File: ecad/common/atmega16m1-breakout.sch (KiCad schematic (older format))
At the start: 17 parts, among them J1 Conn_01x15, J2 Conn_01x15, J3 Conn_02x03_Odd_Even, SW1 SW_Push, U1 ATMEGA16M1-AU, U2 NCP1117-5.0_SOT223, Y1 16MHz

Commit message: wip
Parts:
- removed J1, J2: Conn_01x15, Pin_Headers:Pin_Header_Straight_1x15_Pitch2.54mm, symbol Conn_01x15
- added C9: 100nF, Capacitors_SMD:C_0603, symbol C
- added J?: Conn_01x08, symbol Conn_01x08
- added J?: Conn_01x03, symbol Conn_01x03
- added J? (x2): Conn_01x06, symbol Conn_01x06
- added J?: Conn_01x05, symbol Conn_01x05
- added U3: MCP2561-E/SN, Housings_SOIC:SOIC-8_3.9x4.9mm_Pitch1.27mm, symbol MCP2561-E/SN
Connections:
- net labels added: CAN+, CAN-, RXCAN, TXCAN
- net labels removed: 6, 7
- wire segments 123 -> 135
- no-connect marks 1 -> 2

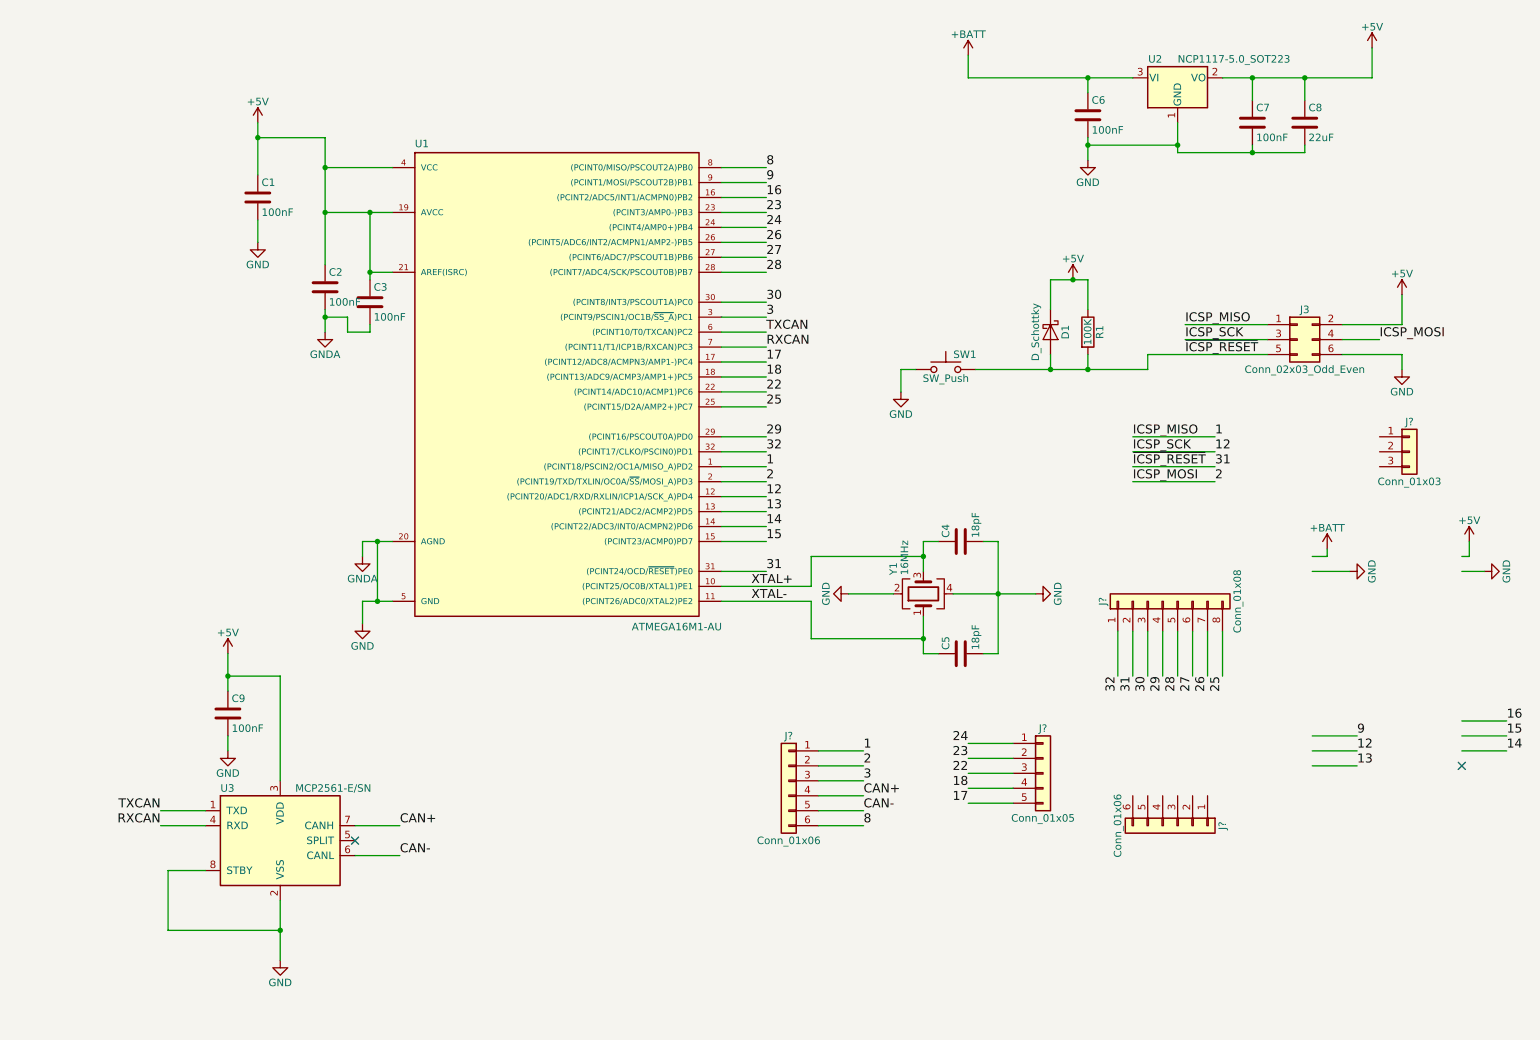
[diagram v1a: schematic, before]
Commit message: Adds CAN Transceiver on atmega16m1 breakout
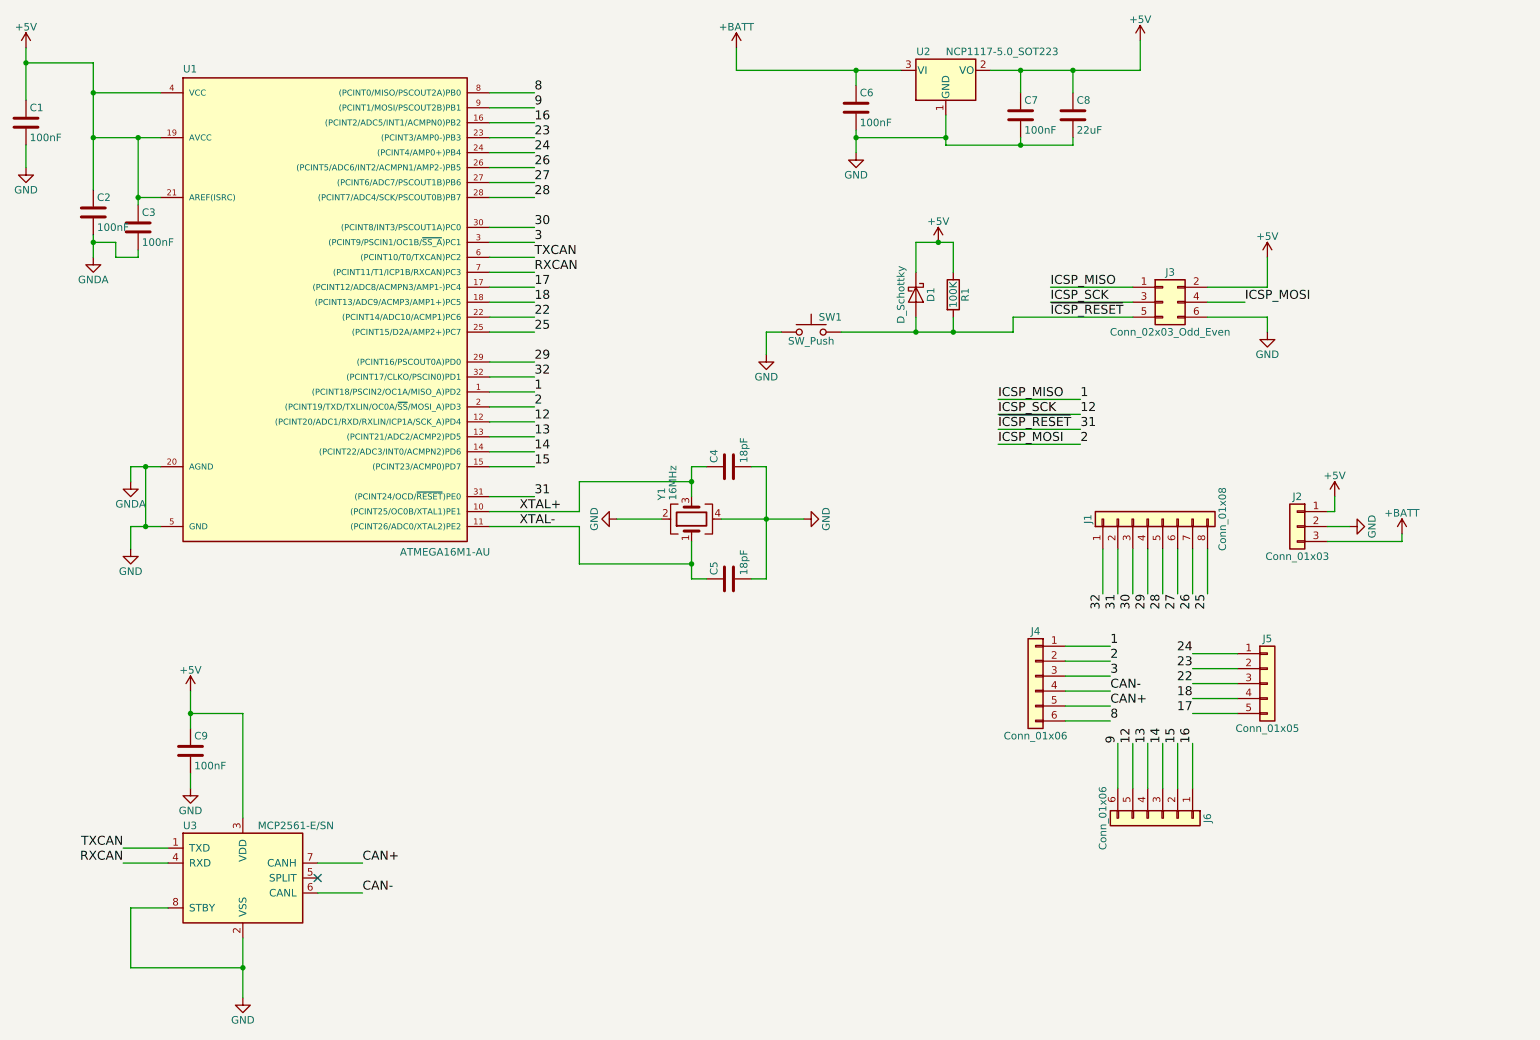
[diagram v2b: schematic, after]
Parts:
- J1: renamed from J?; footprint (none) -> Pin_Headers:Pin_Header_Straight_1x08_Pitch2.54mm
- J2: renamed from J?; footprint (none) -> Pin_Headers:Pin_Header_Straight_1x03_Pitch2.54mm
- J4, J6: renamed from J?; footprint (none) -> Pin_Headers:Pin_Header_Straight_1x06_Pitch2.54mm
- J5: renamed from J?; footprint (none) -> Pin_Headers:Pin_Header_Straight_1x05_Pitch2.54mm
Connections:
- wire segments 135 -> 134
- no-connect marks 2 -> 1
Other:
- moved on the sheet: C1, C2, C3, C4, C5, C6, C7, C8, C9, D1, J1, J2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

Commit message: Updates breakout board
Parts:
- C1, C2, C3, C6, C7, C9: Part Number (none) -> 06035C104KAT2A
- C4, C5: Part Number (none) -> 06031A180KAT2A
- D1: Part Number (none) -> BAT54
- R1: Part Number (none) -> RMCF0603FT10K0
- SW1: Part Number (none) -> 1825910-6
- Y1: Part Number (none) -> FA-238 16.0000MB-C3
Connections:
- net GND: now also C4.1; no longer C4.2
- net XTAL+: now also C4.2; no longer C4.1
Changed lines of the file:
@@
 F 2 "Capacitors_SMD:C_0603" H 888 1200 50  0001 C CNN
 F 3 "" H 850 1350 50  0001 C CNN
+F 4 "06035C104KAT2A" H 850 1350 60  0001 C CNN "Part Number"
 	1    850  1350
 	1    0    0    -1
@@
 F 2 "Capacitors_SMD:C_0603" H 1338 1800 50  0001 C CNN
 F 3 "" H 1300 1950 50  0001 C CNN
+F 4 "06035C104KAT2A" H 1300 1950 60  0001 C CNN "Part Number"
 	1    1300 1950
 	1    0    0    -1
@@
 F 2 "Capacitors_SMD:C_0603" H 1638 1900 50  0001 C CNN
 F 3 "" H 1600 2050 50  0001 C CNN
+F 4 "06035C104KAT2A" H 1600 2050 60  0001 C CNN "Part Number"
 	1    1600 2050
 	1    0    0    -1
@@
 	1300 1450 1750 1450
 $Comp
-L +5V #PWR2
+L +5V #PWR01
 U 1 1 5B852E50
 P 850 850
-F 0 "#PWR2" H 850 700 50  0001 C CNN
+F 0 "#PWR01" H 850 700 50  0001 C CNN
 F 1 "+5V" H 850 990 50  0000 C CNN
 F 2 "" H 850 850 50  0001 C CNN
@@
 Connection ~ 850  950
 $Comp
-L GND #PWR5
+L GND #PWR02
 U 1 1 5B852E84
 P 850 1650
-F 0 "#PWR5" H 850 1400 50  0001 C CNN
+F 0 "#PWR02" H 850 1400 50  0001 C CNN
 F 1 "GND" H 850 1500 50  0000 C CNN
 F 2 "" H 850 1650 50  0001 C CNN
@@
 	850  1650 850  1500
 $Comp
-L GNDA #PWR7
+L GNDA #PWR03
 U 1 1 5B852EBB
 P 1300 2250
-F 0 "#PWR7" H 1300 2000 50  0001 C CNN
+F 0 "#PWR03" H 1300 2000 50  0001 C CNN
 F 1 "GNDA" H 1300 2100 50  0000 C CNN
 F 2 "" H 1300 2250 50  0001 C CNN
@@
 Connection ~ 1300 2150
 $Comp
-L GND #PWR17
+L GND #PWR04
 U 1 1 5B852F69
 P 1550 4200
-F 0 "#PWR17" H 1550 3950 50  0001 C CNN
+F 0 "#PWR04" H 1550 3950 50  0001 C CNN
 F 1 "GND" H 1550 4050 50  0000 C CNN
 F 2 "" H 1550 4200 50  0001 C CNN
@@
 $EndComp
 $Comp
-L GNDA #PWR11
+L GNDA #PWR05
 U 1 1 5B852F94
 P 1550 3750
-F 0 "#PWR11" H 1550 3500 50  0001 C CNN
+F 0 "#PWR05" H 1550 3500 50  0001 C CNN
 F 1 "GNDA" H 1550 3600 50  0000 C CNN
 F 2 "" H 1550 3750 50  0001 C CNN
@@
 F 2 "Crystals:Crystal_SMD_SeikoEpson_FA238-4pin_3.2x2.5mm_HandSoldering" H 5300 4000 50  0001 C CNN
 F 3 "" H 5300 4000 50  0001 C CNN
+F 4 "FA-238 16.0000MB-C3" H 5300 4000 60  0001 C CNN "Part Number"
 	1    5300 4000
 	0    -1   -1   0
@@
 F 2 "Capacitors_SMD:C_0603" H 5588 3500 50  0001 C CNN
 F 3 "" H 5550 3650 50  0001 C CNN
+F 4 "06031A180KAT2A" H 5550 3650 60  0001 C CNN "Part Number"
 	1    5550 3650
-	0    -1   -1   0
+	0    1    1    0
 $EndComp
 $Comp
@@
 F 2 "Capacitors_SMD:C_0603" H 5588 4250 50  0001 C CNN
 F 3 "" H 5550 4400 50  0001 C CNN
+F 4 "06031A180KAT2A" H 5550 4400 60  0001 C CNN "Part Number"
 	1    5550 4400
 	0    -1   -1   0
@@
 Connection ~ 5800 4000
 $Comp
-L GND #PWR14
+L GND #PWR06
 U 1 1 5B853598
 P 6050 4000
-F 0 "#PWR14" H 6050 3750 50  0001 C CNN
+F 0 "#PWR06" H 6050 3750 50  0001 C CNN
 F 1 "GND" H 6050 3850 50  0000 C CNN
 F 2 "" H 6050 4000 50  0001 C CNN
@@
 Connection ~ 5300 4300
 $Comp
-L GND #PWR13
+L GND #PWR07
 U 1 1 5B8539B2
 P 4800 4000
-F 0 "#PWR13" H 4800 3750 50  0001 C CNN
+F 0 "#PWR07" H 4800 3750 50  0001 C CNN
 F 1 "GND" H 4800 3850 50  0000 C CNN
 F 2 "" H 4800 4000 50  0001 C CNN
@@
 F 2 "Capacitors_SMD:C_0603" H 6438 1100 50  0001 C CNN
 F 3 "" H 6400 1250 50  0001 C CNN
+F 4 "06035C104KAT2A" H 6400 1250 60  0001 C CNN "Part Number"
 	1    6400 1250
 	1    0    0    -1
@@
 F 2 "Capacitors_SMD:C_0603" H 7538 1150 50  0001 C CNN
 F 3 "" H 7500 1300 50  0001 C CNN
+F 4 "06035C104KAT2A" H 7500 1300 60  0001 C CNN "Part Number"
 	1    7500 1300
 	1    0    0    -1
 $EndComp
 $Comp
-L +BATT #PWR3
+L +BATT #PWR08
 U 1 1 5B853FF4
 P 5600 850
-F 0 "#PWR3" H 5600 700 50  0001 C CNN
+F 0 "#PWR08" H 5600 700 50  0001 C CNN
 F 1 "+BATT" H 5600 990 50  0000 C CNN
 F 2 "" H 5600 850 50  0001 C CNN
@@
 Connection ~ 7850 1000
 $Comp
-L +5V #PWR1
+L +5V #PWR09
 U 1 1 5B854218
 P 8300 800
-F 0 "#PWR1" H 8300 650 50  0001 C CNN
+F 0 "#PWR09" H 8300 650 50  0001 C CNN
 F 1 "+5V" H 8300 940 50  0000 C CNN
 F 2 "" H 8300 800 50  0001 C CNN
@@
 $EndComp
 $Comp
-L GND #PWR4
+L GND #PWR010
 U 1 1 5B854242
 P 6400 1550
-F 0 "#PWR4" H 6400 1300 50  0001 C CNN
+F 0 "#PWR010" H 6400 1300 50  0001 C CNN
 F 1 "GND" H 6400 1400 50  0000 C CNN
 F 2 "" H 6400 1550 50  0001 C CNN
@@
 Connection ~ 1650 3650
 $Comp
-L +BATT #PWR16
+L +BATT #PWR011
 U 1 1 5B85479A
 P 10050 4100
-F 0 "#PWR16" H 10050 3950 50  0001 C CNN
+F 0 "#PWR011" H 10050 3950 50  0001 C CNN
 F 1 "+BATT" H 10050 4240 50  0000 C CNN
 F 2 "" H 10050 4100 50  0001 C CNN
@@
 $EndComp
 $Comp
-L +5V #PWR12
+L +5V #PWR012
 U 1 1 5B854806
 P 9600 3850
-F 0 "#PWR12" H 9600 3700 50  0001 C CNN
+F 0 "#PWR012" H 9600 3700 50  0001 C CNN
 F 1 "+5V" H 9600 3990 50  0000 C CNN
 F 2 "" H 9600 3850 50  0001 C CNN
@@
 	9600 3950 9550 3950
 $Comp
-L GND #PWR15
+L GND #PWR013
 U 1 1 5B85498D
 P 9700 4050
-F 0 "#PWR15" H 9700 3800 50  0001 C CNN
+F 0 "#PWR013" H 9700 3800 50  0001 C CNN
 F 1 "GND" H 9700 3900 50  0000 C CNN
 F 2 "" H 9700 4050 50  0001 C CNN
@@
 ICSP_MOSI
 $Comp
-L GND #PWR9
+L GND #PWR014
 U 1 1 5B855C2C
 P 9150 2750
-F 0 "#PWR9" H 9150 2500 50  0001 C CNN
+F 0 "#PWR014" H 9150 2500 50  0001 C CNN
 F 1 "GND" H 9150 2600 50  0000 C CNN
 F 2 "" H 9150 2750 50  0001 C CNN
@@
 $EndComp
 $Comp
-L +5V #PWR8
+L +5V #PWR015
 U 1 1 5B855C5C
 P 9150 2250
-F 0 "#PWR8" H 9150 2100 50  0001 C CNN
+F 0 "#PWR015" H 9150 2100 50  0001 C CNN
 F 1 "+5V" H 9150 2390 50  0000 C CNN
 F 2 "" H 9150 2250 50  0001 C CNN
@@
 F 2 "Diodes_SMD:D_SOT-23_ANK" H 6800 2500 50  0001 C CNN
 F 3 "" H 6800 2500 50  0001 C CNN
+F 4 "BAT54" H 6800 2500 60  0001 C CNN "Part Number"
 	1    6800 2500
 	0    1    1    0
@@
 F 2 "Buttons_Switches_THT:SW_PUSH_6mm" H 6100 2950 50  0001 C CNN
 F 3 "" H 6100 2950 50  0001 C CNN
+F 4 "1825910-6" H 6100 2750 60  0001 C CNN "Part Number"
 	1    6100 2750
 	1    0    0    -1
@@
 F 2 "Resistors_SMD:R_0603_HandSoldering" V 6980 2500 50  0001 C CNN
 F 3 "" H 7050 2500 50  0001 C CNN
+F 4 "RMCF0603FT10K0" H 7050 2500 60  0001 C CNN "Part Number"
 	1    7050 2500
 	1    0    0    -1
 $EndComp
 $Comp
-L GND #PWR10
+L GND #PWR016
 U 1 1 5B8561C9
 P 5800 2900
-F 0 "#PWR10" H 5800 2650 50  0001 C CNN
+F 0 "#PWR016" H 5800 2650 50  0001 C CNN
 F 1 "GND" H 5800 2750 50  0000 C CNN
 F 2 "" H 5800 2900 50  0001 C CNN
@@
 Connection ~ 7050 2750
 $Comp
-L +5V #PWR6
+L +5V #PWR017
 U 1 1 5B85645E
 P 6950 2150
-F 0 "#PWR6" H 6950 2000 50  0001 C CNN
+F 0 "#PWR017" H 6950 2000 50  0001 C CNN
 F 1 "+5V" H 6950 2290 50  0000 C CNN
 F 2 "" H 6950 2150 50  0001 C CNN
@@
 	2300 6800 2300 7200
 $Comp
-L GND #PWR20
+L GND #PWR018
 U 1 1 5B87A4DF
 P 2300 7200
-F 0 "#PWR20" H 2300 6950 50  0001 C CNN
+F 0 "#PWR018" H 2300 6950 50  0001 C CNN
 F 1 "GND" H 2300 7050 50  0000 C CNN
 F 2 "" H 2300 7200 50  0001 C CNN
@@
 F 2 "Capacitors_SMD:C_0603" H 1988 5400 50  0001 C CNN
 F 3 "" H 1950 5550 50  0001 C CNN
+F 4 "06035C104KAT2A" H 1950 5550 60  0001 C CNN "Part Number"
 	1    1950 5550
 	1    0    0    -1
@@
 	2300 5300 2300 6000
 $Comp
-L GND #PWR19
+L GND #PWR019
 U 1 1 5B87A93E
 P 1950 5800
-F 0 "#PWR19" H 1950 5550 50  0001 C CNN
+F 0 "#PWR019" H 1950 5550 50  0001 C CNN
 F 1 "GND" H 1950 5650 50  0000 C CNN
 F 2 "" H 1950 5800 50  0001 C CNN
@@
 	1950 5800 1950 5700
 $Comp
-L +5V #PWR18
+L +5V #PWR020
 U 1 1 5B87ABCF
 P 1950 5150
-F 0 "#PWR18" H 1950 5000 50  0001 C CNN
+F 0 "#PWR020" H 1950 5000 50  0001 C CNN
 F 1 "+5V" H 1950 5290 50  0000 C CNN
 F 2 "" H 1950 5150 50  0001 C CNN
